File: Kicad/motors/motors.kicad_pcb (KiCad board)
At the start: 2 copper layers, 80 x 100 mm, 64 parts, among them IC101 TLV1117-50, IC201 PIC16F1778-IP, IC301 MCP2221A-ISL, K101 Battery, K201 MCU 1, K202 MCU 2, K203 ICSP, K301 FRONT, K302 MICRO USB B, K303 M20-782084x, K304 M20-782084x, K305 SERVO LEFT, K306 SERVO RIGHT, T101 DMP2305U, T102 DMP2305U

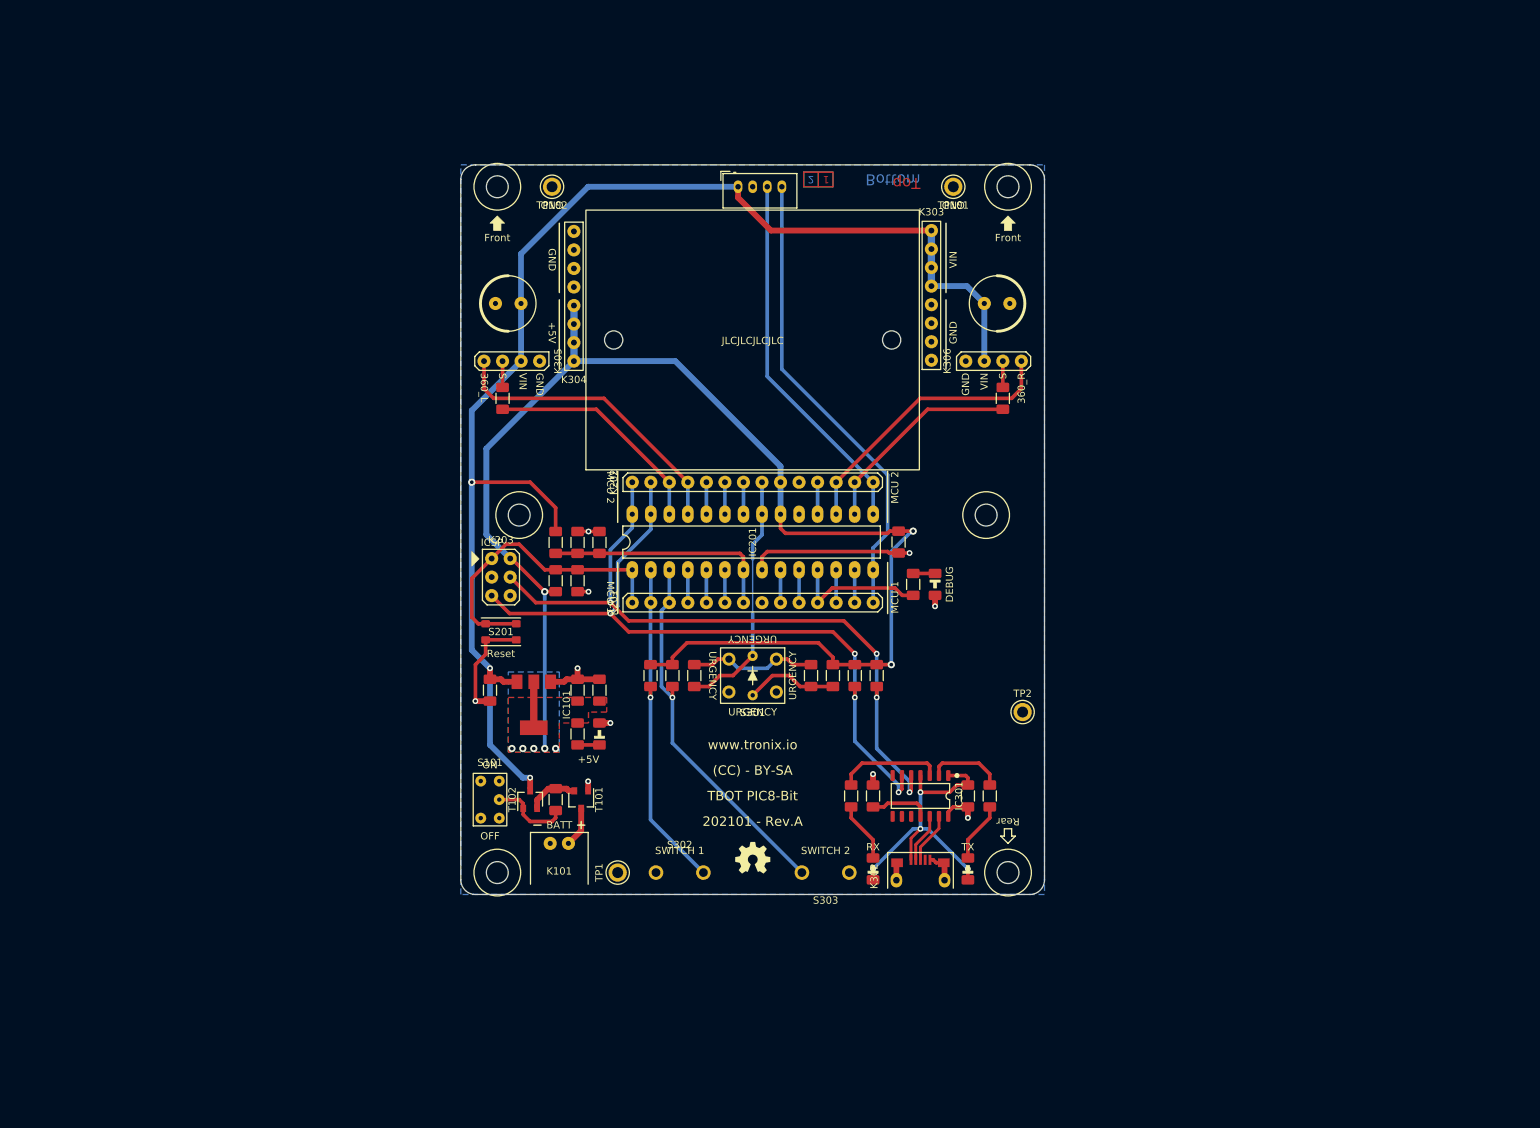
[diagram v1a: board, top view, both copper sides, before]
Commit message: Update Motors
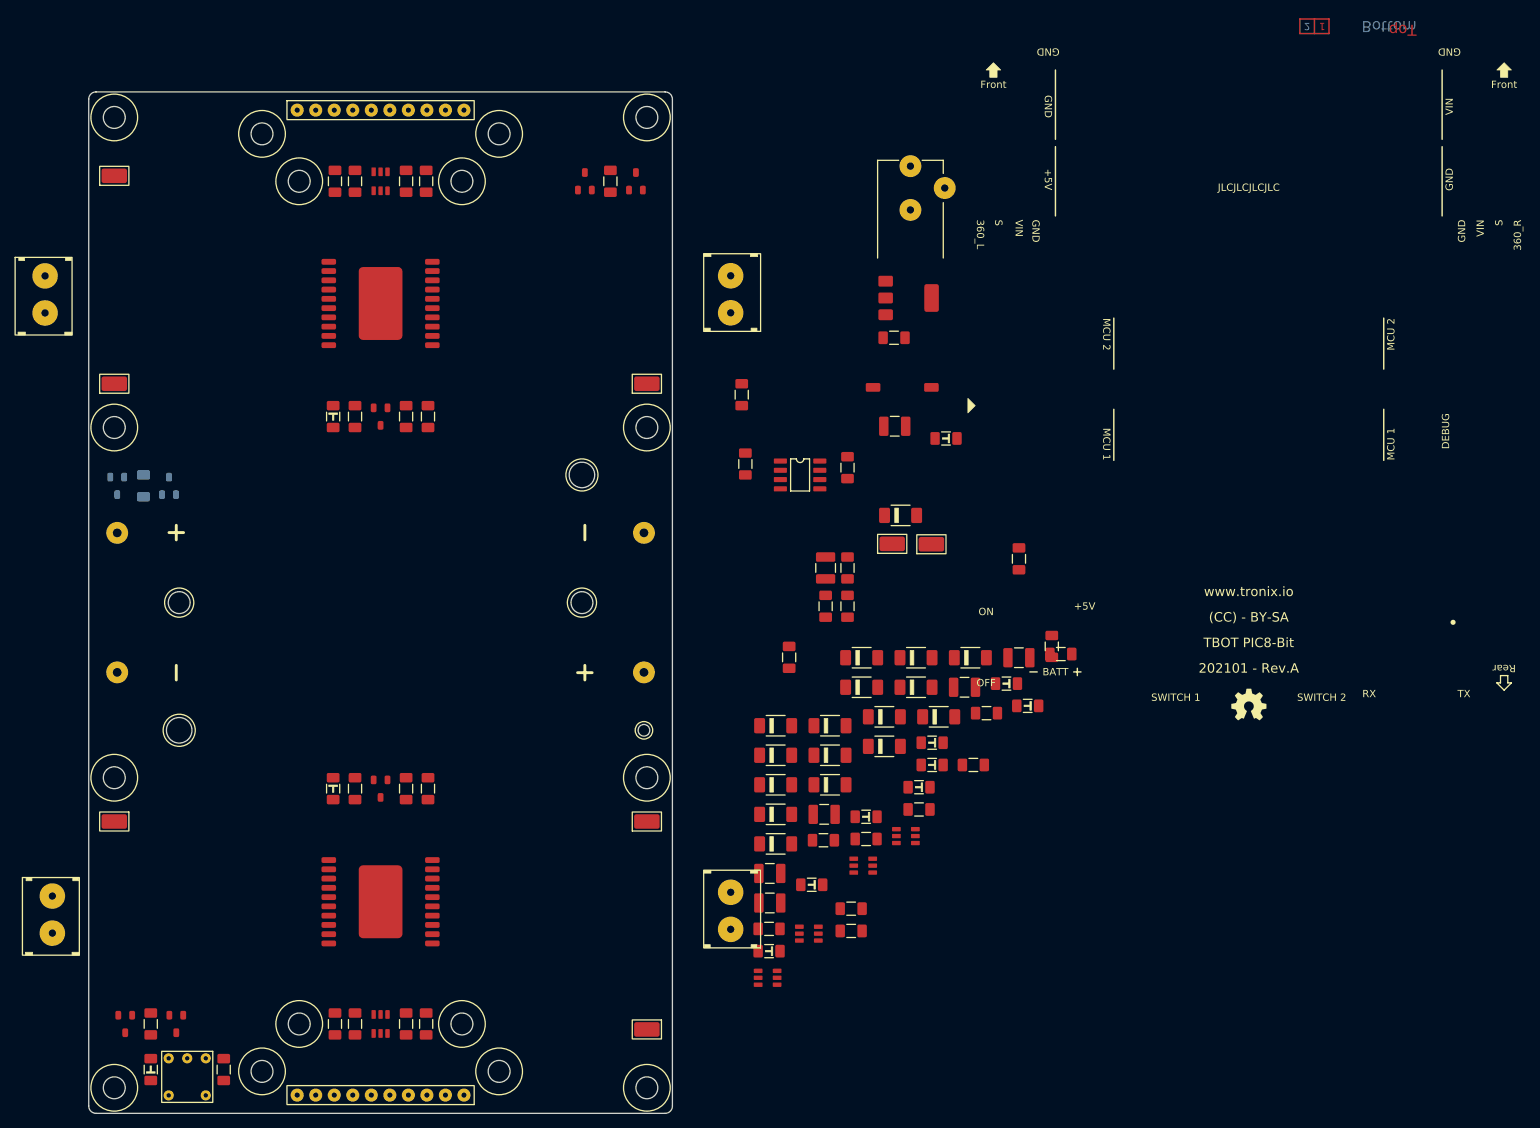
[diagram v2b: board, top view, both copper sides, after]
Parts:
- removed BB301: BREADBOARD-170, tronixALL:BREADBOARD-170
- removed C102, C104: 10µ, tronixALL:CAPACITOR_1206
- removed C103: 100n, tronixALL:CAPACITOR_1206
- removed H1, H2, H3, H4, H5, H6: MOUNTING-HOLE-MASK-3MM, tronixALL:M3-MASK
- removed IC101: TLV1117-50, tronixALL:SOT-223-3
- removed K101: Battery, tronixALL:MOLEX-5268-02
- removed K303, K304: M20-782084x, tronixALL:M20-782084x
- removed K305: SERVO LEFT, tronixALL:M20-999044x
- removed K306: SERVO RIGHT, tronixALL:M20-999044x
- removed LED302: UTX, tronixALL:LED_1206
- removed LED305: DEBUG, tronixALL:LED_1206
- removed R310, R311: 10K, tronixALL:RESISTOR_1206
- removed R314: 5K6, tronixALL:RESISTOR_1206
- removed S101: ON/OFF, tronixALL:E-SWITCH-200USPXT1A1M2RE
- removed S201: Reset, tronixALL:ALPS-SKRPAC
- removed S301: URGENCY, tronixALL:E-SWITCH-TL1240XQ1JXXX
- removed S302: SWITCH 1, tronixALL:CK-PTS635S-THT
- removed S303: SWITCH 2, tronixALL:CK-PTS635S-THT
- removed T101, T102: DMP2305U, tronixALL:SOT-23-3
- removed TP1, TP2: GND, tronixALL:KEYSTONE-5006
- added BT100: 2x18650, tronixio:KEYSTONE-1049, F.Cu at (89.0, 110.0)
- added C100: 100n, tronixio:CAPACITOR-1206, F.Cu at (153.5, 151.9)
- added C205: 100n, tronixio:CAPACITOR-1206, F.Cu at (172.1, 125.2)
- added C206: 100n, tronixio:CAPACITOR-1206, F.Cu at (155.6, 142.4)
- added C209: 100n, tronixio:CAPACITOR-1206, F.Cu at (170.2, 132.2)
- added C210: 100n, tronixio:CAPACITOR-1206, F.Cu at (142.2, 154.7)
- added C211: 1µ, tronixio:CAPACITOR-1206, F.Cu at (85.5, 84.5)
- added C212: 1µ, tronixio:CAPACITOR-1206, F.Cu at (92.5, 84.5)
- added C305: 1µ, tronixio:CAPACITOR-1206, F.Cu at (85.5, 135.5)
- added C306: 1µ, tronixio:CAPACITOR-1206, F.Cu at (92.5, 135.5)
- added D100: PMEG3030, tronixio:SOD-128, F.Cu at (160.3, 98.0)
- added D201: PMEG3030, tronixio:SOD-128, F.Cu at (143.2, 143.1)
- added D202: PMEG3030, tronixio:SOD-128, F.Cu at (154.9, 117.5)
- added D203: PMEG3030, tronixio:SOD-128, F.Cu at (162.4, 117.5)
- added D204: PMEG3030, tronixio:SOD-128, F.Cu at (169.8, 117.5)
- added D205: PMEG3030, tronixio:SOD-128, F.Cu at (143.2, 135.0)
- added D206: PMEG3030, tronixio:SOD-128, F.Cu at (158.1, 129.7)
- added D207: PMEG3030, tronixio:SOD-128, F.Cu at (165.5, 125.7)
- added D208: PMEG3030, tronixio:SOD-128, F.Cu at (143.2, 126.9)
- added D209: PMEG3030, tronixio:SOD-128, F.Cu at (150.6, 130.9)
- added D210: PMEG3030, tronixio:SOD-128, F.Cu at (158.1, 125.7)
- added D211: PMEG3030, tronixio:SOD-128, F.Cu at (154.9, 121.6)
- added D212: PMEG3030, tronixio:SOD-128, F.Cu at (150.6, 135.0)
- added D213: PMEG3030, tronixio:SOD-128, F.Cu at (150.6, 126.9)
- added D214: PMEG3030, tronixio:SOD-128, F.Cu at (143.2, 139.0)
- added D215: PMEG3030, tronixio:SOD-128, F.Cu at (143.2, 130.9)
- added D216: PMEG3030, tronixio:SOD-128, F.Cu at (162.4, 121.6)
- added H101: MOUNTING-HOLE-MASK-3MM, tronixio:M3-MASK, F.Cu at (52.5, 176.5)
- added H102: MOUNTING-HOLE-MASK-3MM, tronixio:M3-MASK, F.Cu at (72.8, 174.2)
- added H103: MOUNTING-HOLE-MASK-3MM, tronixio:M3-MASK, F.Cu at (77.8, 167.8)
- added H104: MOUNTING-HOLE-MASK-3MM, tronixio:M3-MASK, F.Cu at (100.2, 167.8)
- added H105: MOUNTING-HOLE-MASK-3MM, tronixio:M3-MASK, F.Cu at (105.2, 174.2)
- added H106: MOUNTING-HOLE-MASK-3MM, tronixio:M3-MASK, F.Cu at (125.5, 176.5)
- added H107: MOUNTING-HOLE-MASK-3MM, tronixio:M3-MASK, F.Cu at (125.5, 134.0)
- added H108: MOUNTING-HOLE-MASK-3MM, tronixio:M3-MASK, F.Cu at (125.5, 86.0)
- added H109: MOUNTING-HOLE-MASK-3MM, tronixio:M3-MASK, F.Cu at (125.5, 43.5)
- added H110: MOUNTING-HOLE-MASK-3MM, tronixio:M3-MASK, F.Cu at (105.2, 45.8)
- added H111: MOUNTING-HOLE-MASK-3MM, tronixio:M3-MASK, F.Cu at (100.2, 52.2)
- added H112: MOUNTING-HOLE-MASK-3MM, tronixio:M3-MASK, F.Cu at (77.8, 52.2)
- added H113: MOUNTING-HOLE-MASK-3MM, tronixio:M3-MASK, F.Cu at (72.8, 45.8)
- added H114: MOUNTING-HOLE-MASK-3MM, tronixio:M3-MASK, F.Cu at (52.5, 43.5)
- added H115: MOUNTING-HOLE-MASK-3MM, tronixio:M3-MASK, F.Cu at (52.5, 86.0)
- added H116: MOUNTING-HOLE-MASK-3MM, tronixio:M3-MASK, F.Cu at (52.5, 134.0)
- added IC100: BQ2057W, tronixio:SOIC-08, F.Cu at (146.5, 92.5)
- added IC202: SN74LVC1G19, tronixio:SOT-23-6, F.Cu at (142.1, 161.4)
- added IC203: SN74LVC1G19, tronixio:SOT-23-6, F.Cu at (155.2, 146.1)
- added IC204: L298P, tronixio:zzzSOPOWER-20, F.Cu at (89.0, 151.0)
- added IC205: SN74LVC1G19, tronixio:SOT-23-6, F.Cu at (147.7, 155.4)
- added IC206: SN74LVC1G19, tronixio:SOT-23-6, F.Cu at (161.0, 142.0)
- added IC207: LM3480-50, tronixio:SOT-23-3, F.Cu at (89.0, 84.5)
- added IC302: SN74LVC2G17, tronixio:SOT-23-6, F.Cu at (89.0, 167.8)
- added IC307: LM3480-33, tronixio:SOT-23-3, F.Cu at (89.0, 135.5)
- added K100: Charger, tronixio:CUI-PJ-102AH, F.Cu at (161.6, 50.2)
- added K204: MOTOR 3, tronixio:CUI-TB006-508-02BE, F.Cu at (44.0, 150.2)
- added LED100: Charging, tronixio:LED-1206, F.Cu at (166.5, 87.5)
- added LED201: Red, tronixio:LED-1206, F.Cu at (164.6, 132.2)
- added LED202: Red, tronixio:LED-1206, F.Cu at (162.8, 135.3)
- added LED203: Red, tronixio:LED-1206, F.Cu at (164.6, 129.2)
- added LED204: Red, tronixio:LED-1206, F.Cu at (177.7, 124.2)
- added LED205: Red, tronixio:LED-1206, F.Cu at (155.6, 139.3)
- added LED206: Red, tronixio:LED-1206, F.Cu at (142.2, 157.8)
- added LED207: Red, tronixio:LED-1206, F.Cu at (174.8, 121.1)
- added LED208: Red, tronixio:LED-1206, F.Cu at (148.1, 148.7)
- added LED209: +5V, tronixio:LED-1206, F.Cu at (82.5, 84.5)
- added Q100: STN790A, tronixio:SOT-223-3, F.Cu at (161.4, 68.2)
- added Q101: DMP2305U, tronixio:SOT-23-3, B.Cu at (52.9, 94.0)
- added Q102: DMP2305U, tronixio:SOT-23-3, B.Cu at (60.0, 94.0)
- added Q301: BC846B, tronixio:SOT-23-3, F.Cu at (117.0, 52.2)
- added Q302: BC846B, tronixio:SOT-23-3, F.Cu at (61.0, 167.8)
- added Q303: BC846B, tronixio:SOT-23-3, F.Cu at (124.0, 52.2)
- added Q304: BC846B, tronixio:SOT-23-3, F.Cu at (54.0, 167.8)
- added R100: 0Ω1, tronixio:RESISTOR-1210, F.Cu at (159.5, 85.8)
- added R105: 10K, tronixio:RESISTOR-1206, F.Cu at (159.4, 73.7)
- added R106: 36K, tronixio:RESISTOR-1206, F.Cu at (153.5, 155.0)
- added R107: 15K, tronixio:RESISTOR-1206, F.Cu at (67.5, 174.0)
- added R202: 10K, tronixio:RESISTOR-1206, F.Cu at (149.7, 142.6)
- added R203: 10K, tronixio:RESISTOR-1206, F.Cu at (182.2, 117.0)
- added R204: 0Ω5, tronixio:RESISTOR-1210, F.Cu at (176.5, 117.5)
- added R205: 0Ω5, tronixio:RESISTOR-1210, F.Cu at (169.0, 121.6)
- added R206: 10K, tronixio:RESISTOR-1206, F.Cu at (162.8, 138.3)
- added R207: 10K, tronixio:RESISTOR-1206, F.Cu at (138.5, 81.5)
- added R208: 10K, tronixio:RESISTOR-1210, F.Cu at (149.8, 139.0)
- added R209: 0Ω5, tronixio:RESISTOR-1210, F.Cu at (142.3, 147.1)
- added R210: 0Ω5, tronixio:RESISTOR-1210, F.Cu at (142.3, 151.2)
- added R211: 12K, tronixio:RESISTOR-1206, F.Cu at (95.5, 84.5)
- added S100: On/Off, tronixio:zzzE-SWITCH-200USPXT1A1M6RE, F.Cu at (62.5, 175.0)
- added TH100: 10K, tronixio:THERMISTOR, F.Cu at (160.5, 80.5)
- added TP100: HARWIN-S1751, tronixio:zzzHARWIN-S1751, F.Cu at (52.5, 80.0)
- added TP103: HARWIN-S1751, tronixio:zzzHARWIN-S1751, F.Cu at (52.5, 51.5)
- added TP104: HARWIN-S1751, tronixio:zzzHARWIN-S1751, F.Cu at (159.1, 101.9)
- added TP105: HARWIN-S1751, tronixio:zzzHARWIN-S1751, F.Cu at (164.5, 102.0)
- added TP201: HARWIN-S1751, tronixio:zzzHARWIN-S1751, F.Cu at (125.5, 80.0)
- added TP301: HARWIN-S1751, tronixio:zzzHARWIN-S1751, F.Cu at (125.5, 140.0)
- C101: value 100n -> 1µ; footprint tronixALL:CAPACITOR_1206 -> tronixio:CAPACITOR-1206
- C201, C202, C301: footprint tronixALL:CAPACITOR_1206 -> tronixio:CAPACITOR-1206
- C302: value 470n -> 1µ; footprint tronixALL:CAPACITOR_1206 -> tronixio:CAPACITOR-1206
- C303: value UVZ-220U-25V -> 100n; footprint tronixALL:CAPACITOR-ELECTROLYTIC-RADIAL-080-115-035 -> tronixio:CAPACITOR-1206
- C304: value UVZ-220U-25V -> 1µ; footprint tronixALL:CAPACITOR-ELECTROLYTIC-RADIAL-080-115-035 -> tronixio:CAPACITOR-1206
- IC201: value PIC16F1778-IP -> L298P; footprint tronixALL:DIP-28-W762 -> tronixio:zzzSOPOWER-20
- IC301: value MCP2221A-ISL -> SN74LVC2G17; footprint tronixALL:SOIC-SL-14 -> tronixio:SOT-23-6
- K201: value MCU 1 -> MOTOR 1; footprint tronixALL:M20-999144x -> tronixio:CUI-TB006-508-02BE
- K202: value MCU 2 -> MOTOR 2; footprint tronixALL:M20-999144x -> tronixio:CUI-TB006-508-02BE
- K203: value ICSP -> MOTOR 4; footprint tronixALL:M20-998034x -> tronixio:CUI-TB006-508-02BE
- K301: value FRONT -> Front; footprint tronixALL:JST-PH-B4B-K -> tronixio:zzHARWIN-M20-782104x
- K302: value MICRO USB B -> Rear; footprint tronixALL:FCI-USB-TYPE-B-MICRO-THT -> tronixio:zzHARWIN-M20-782104x
- LED101: footprint tronixALL:LED_1206 -> tronixio:LED-1206
- LED301: value URX -> +3V3; footprint tronixALL:LED_1206 -> tronixio:LED-1206
- R101: value 7K5 -> 0Ω1; footprint tronixALL:RESISTOR_1206 -> tronixio:RESISTOR-1210
- R102: value 100K -> 1K; footprint tronixALL:RESISTOR_1206 -> tronixio:RESISTOR-1206
- R103, R201: footprint tronixALL:RESISTOR_1206 -> tronixio:RESISTOR-1206
- R104: value 5K6 -> 1M; footprint tronixALL:RESISTOR_1206 -> tronixio:RESISTOR-1206; moved to B.Cu
- R301, R302: value 100K -> 10K; footprint tronixALL:RESISTOR_1206 -> tronixio:RESISTOR-1206
- R303: value 220R -> 10K; footprint tronixALL:RESISTOR_1206 -> tronixio:RESISTOR-1206
- R304: value 150R -> 10K; footprint tronixALL:RESISTOR_1206 -> tronixio:RESISTOR-1206
- R305, R306: value 5K6 -> 2K2; footprint tronixALL:RESISTOR_1206 -> tronixio:RESISTOR-1206
- R307: value 300R -> 33Ω; footprint tronixALL:RESISTOR_1206 -> tronixio:RESISTOR-1206
- R308: value 220R -> 33Ω; footprint tronixALL:RESISTOR_1206 -> tronixio:RESISTOR-1206
- R309: value 220R -> 6K8; footprint tronixALL:RESISTOR_1206 -> tronixio:RESISTOR-1206
- TP101, TP102: value GND -> HARWIN-S1751; footprint tronixALL:KEYSTONE-5006 -> tronixio:zzzHARWIN-S1751
- moved C304 152.3 mm to (57.5, 167.8), turned to -90 degrees
- moved TP101 144.2 mm to (52.5, 140.0)
- moved C301 119.0 mm to (85.5, 52.2)
- moved TP102 116.2 mm to (125.5, 168.5)
- moved IC301 112.1 mm to (89.0, 52.2), turned to 90 degrees
- moved R305 104.0 mm to (92.5, 52.2)
- moved R301 100.5 mm to (82.8, 52.2), turned to -90 degrees
- moved C303 99.7 mm to (92.5, 167.8), turned to 90 degrees
- moved R309 95.2 mm to (95.5, 135.5), turned to -90 degrees
- moved R306 92.4 mm to (85.5, 167.8), turned to 90 degrees
- moved K201 92.1 mm to (43.0, 65.2), turned to -90 degrees
- moved K302 90.5 mm to (77.6, 177.5)
- moved R303 87.7 mm to (95.2, 52.2), turned to -90 degrees
- moved R304 80.9 mm to (82.8, 167.8), turned to 90 degrees
- moved LED101 76.8 mm to (57.5, 174.0)
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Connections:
- C101 pad 1: RA5/BATTERY_SENSE -> VBAT
- C202 pad 1: ~{MCLR} -> VIN
- C301 pad 1: VUSB -> +3V3
- C302 pad 1: Net-(C302-Pad1) -> +3V3
- C303 pad 1: VIN -> +3V3
- C304 pad 1: VIN -> +3V3
- IC201 pad 1: ~{MCLR} -> GND
- IC201 pad 10: RA6 -> GND
- IC201 pad 11: RC0/LED -> GND
- IC201 pad 12: RC1 -> +5V
- IC201 pad 13: RC2/ENABLE -> Net-(IC203-Pad6)
- IC201 pad 14: RC3/TRIGGER -> /Driver/STOP
- IC201 pad 15: RC4/ECHO -> Net-(IC203-Pad4)
- IC201 pad 16: RC5/SERVO_R -> Net-(D203-Pad2)
- IC201 pad 17: RC6/360_R -> Net-(D204-Pad2)
- IC201 pad 18: RC7 -> (no net)
- IC201 pad 19: GND -> /Driver/M2_SENSE
- IC201 pad 2: RA0/SWITCH_1 -> /Driver/M1_SENSE
- IC201 pad 20: +5V -> GND
- IC201 pad 21: RB0/URGENCY -> (no net)
- IC201 pad 3: RA1/SWITCH_2 -> (no net)
- IC201 pad 4: RA2 -> Net-(D201-Pad2)
- IC201 pad 5: RA3 -> Net-(D202-Pad2)
- IC201 pad 6: RA4 -> VIN
- IC201 pad 7: RA5/BATTERY_SENSE -> Net-(IC202-Pad6)
- IC201 pad 8: GND -> /Driver/STOP
- IC201 pad 9: RA7 -> Net-(IC202-Pad4)
- IC301 pad 1: VUSB -> Net-(IC301-Pad1)
- IC301 pad 2: Net-(IC301-Pad2) -> GND
- IC301 pad 4: VUSB -> ENCODER_M2
- IC301 pad 5: RB7/PGD/UTX -> (no net)
- IC301 pad 6: RB6/PGC/URX -> +3V3
- K201 pad 1: ~{MCLR} -> Net-(D201-Pad2)
- K201 pad 2: RA0/SWITCH_1 -> Net-(D202-Pad2)
- K202 pad 1: RB7/PGD/UTX -> Net-(D203-Pad2)
- K202 pad 2: RB6/PGC/URX -> Net-(D204-Pad2)
- K203 pad 1: ~{MCLR} -> Net-(D209-Pad2)
- K203 pad 2: +5V -> Net-(D210-Pad2)
- K301 pad 2: GND -> /Driver/M2_SENSE
- K301 pad 3: RC4/ECHO -> /Driver/M2_SPEED
- K301 pad 4: RC3/TRIGGER -> ENCODER_M12
- K302 pad 1: VUSB -> VIN
- K302 pad 2: Net-(IC301-Pad12) -> /Driver/M3_SENSE
- K302 pad 3: Net-(IC301-Pad13) -> /Driver/M3_SPEED
- K302 pad 4: (no net) -> ENCODER_M34
- K302 pad 5: GND -> ENCODER_M3
- K302 pad 6: GND -> ENCODER_M4
- LED301 pad 1: Net-(LED301-Pad1) -> GND
- LED301 pad 2: VUSB -> Net-(LED301-Pad2)
- R101 pad 1: RA5/BATTERY_SENSE -> VCC
- R101 pad 2: VIN -> Net-(IC100-Pad1)
- R103 pad 1: GND -> VCC
- R103 pad 2: RA5/BATTERY_SENSE -> Net-(IC100-Pad4)
- R104 pad 1: Net-(LED101-Pad2) -> Net-(R104-Pad1)
- R104 pad 2: +5V -> Net-(Q101-Pad2)
- R201 pad 1: ~{MCLR} -> +3V3
- R201 pad 2: +5V -> /Driver/BRAKE
- R301 pad 1: RB7/PGD/UTX -> +3V3
- R301 pad 2: +5V -> Net-(IC301-Pad1)
- R302 pad 1: RB6/PGC/URX -> +3V3
- R302 pad 2: +5V -> Net-(IC302-Pad1)
- R303 pad 1: Net-(R303-Pad1) -> +3V3
- R303 pad 2: +5V -> Net-(IC301-Pad3)
- R304 pad 1: Net-(R304-Pad1) -> +3V3
- R304 pad 2: Net-(R303-Pad1) -> Net-(IC302-Pad3)
- R305 pad 1: Net-(IC301-Pad3) -> ENCODER_M12
- R305 pad 2: Net-(LED301-Pad1) -> Net-(Q301-Pad1)
- R306 pad 1: Net-(IC301-Pad2) -> ENCODER_M34
- R307 pad 1: Net-(R304-Pad1) -> Net-(Q301-Pad2)
- R307 pad 2: RB0/URGENCY -> GND
- R308 pad 1: RB5/SERVO_L -> Net-(Q302-Pad2)
- R308 pad 2: Net-(K305-Pad3) -> GND
- R309 pad 1: RC5/SERVO_R -> +3V3
- R309 pad 2: Net-(K306-Pad3) -> Net-(LED301-Pad2)
- TP101 pad 1: GND -> VIN
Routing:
- net +5V: track 194.5 -> 0.00 mm, vias 8 -> 0
- net VIN: track 188.5 -> 0.00 mm, vias 3 -> 0
- net RB6/PGC/URX: track 98.8 -> 0.00 mm, vias 4 -> 0
- net RB7/PGD/UTX: track 97.1 -> 0.00 mm, vias 4 -> 0
- net GND: track 67.8 -> 0.00 mm, vias 10 -> 0
- net RC3/TRIGGER: track 63.8 -> 0.00 mm
- net RA1/SWITCH_2: track 51.4 -> 0.00 mm, vias 1 -> 0
- net RC4/ECHO: track 50.9 -> 0.00 mm
- net RA0/SWITCH_1: track 46.5 -> 0.00 mm, vias 1 -> 0
- net VUSB: track 43.4 -> 0.00 mm, vias 4 -> 0
- net ~{MCLR}: track 41.7 -> 0.00 mm
- net RB4/360_L: track 41.4 -> 0.00 mm
- net RC6/360_R: track 38.9 -> 0.00 mm
- net RB0/URGENCY: track 34.1 -> 0.00 mm
- net RA5/BATTERY_SENSE: track 32.2 -> 0.00 mm
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- removed copper zone on B.Cu, net +5V
- removed copper zone on F.Cu, net +5V
- removed copper zone on B.Cu, net GND
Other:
- board size 80 x 100 mm -> 80 x 140 mm
- board text removed: "URGENCY"

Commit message: Update Motor
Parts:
- removed Q101, Q102: DMP2305U, tronixio:SOT-23-3
- removed TP104, TP105: HARWIN-S1751, tronixio:zzzHARWIN-S1751
- added C203: UVZ-470U-35V, tronixio:zzzCAPACITOR-ELECTROLYTIC-RADIAL-100-160-050, F.Cu at (65.0, 72.5)
- added C204: UVZ-470U-35V, tronixio:zzzCAPACITOR-ELECTROLYTIC-RADIAL-100-160-050, F.Cu at (113.0, 72.5)
- added C207: UVZ-470U-35V, tronixio:zzzCAPACITOR-ELECTROLYTIC-RADIAL-100-160-050, F.Cu at (65.0, 127.5)
- added C208: UVZ-470U-35V, tronixio:zzzCAPACITOR-ELECTROLYTIC-RADIAL-100-160-050, F.Cu at (113.0, 127.5)
- added H117: MOUNTING-HOLE-MASK-3MM, tronixio:M3.5, F.Cu at (75.0, 127.0)
- added H118: MOUNTING-HOLE-MASK-3MM, tronixio:M3.5, F.Cu at (103.0, 127.0)
- added H119: MOUNTING-HOLE-MASK-3MM, tronixio:M3.5, F.Cu at (103.0, 73.0)
- added H120: MOUNTING-HOLE-MASK-3MM, tronixio:M3.5, F.Cu at (75.0, 73.0)
- added IC303: OPB610, tronixio:zzzOPB-610, B.Cu at (67.5, 42.2)
- added IC304: OPB610, tronixio:zzzOPB-610, B.Cu at (110.5, 157.8)
- added IC305: OPB610, tronixio:zzzOPB-610, B.Cu at (110.5, 42.2)
- added IC306: OPB610, tronixio:zzzOPB-610, B.Cu at (67.5, 157.8)
- added T101: DMP2305U, tronixio:SOT-23-3, B.Cu at (52.9, 84.0)
- added T102: DMP2305U, tronixio:SOT-23-3, B.Cu at (60.0, 84.0)
- C100, C101, C302, C304, D100, IC100, LED100, Q100, R100, R101, R102, R103, R105, R106, R202, R203, R206, R207, TH100: moved to B.Cu
- K100: footprint tronixio:CUI-PJ-102AH -> tronixio:zzzCUI-PJ-002AH-SMT-TR; moved to B.Cu
- R208: footprint tronixio:RESISTOR-1210 -> tronixio:RESISTOR-1206
- moved G*** 142.8 mm to (66.0, 109.0)
- moved G*** 137.8 mm to (89.0, 110.5)
- moved LED201 137.2 mm to (54.0, 51.0)
- moved LED202 129.3 mm to (54.0, 65.5), turned to 180 degrees
- moved LED207 124.1 mm to (54.0, 149.5)
- moved R202 122.9 mm to (54.0, 65.5), turned to 180 degrees
- moved D201 120.2 mm to (62.5, 54.0), turned to -90 degrees
- moved R204 119.5 mm to (75.0, 54.6), turned to 180 degrees
- moved IC202 117.9 mm to (75.0, 64.5)
- moved R308 116.2 mm to (57.5, 157.8), turned to -90 degrees
- moved C209 115.0 mm to (75.0, 67.8), turned to 180 degrees
- moved D206 113.1 mm to (67.5, 62.0), turned to -90 degrees
- moved D205 108.8 mm to (62.5, 62.0), turned to -90 degrees
- moved R207 108.5 mm to (54.0, 149.5), turned to 0 degrees
- moved D202 108.1 mm to (67.5, 54.0), turned to -90 degrees
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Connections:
- net Net-(D203-Pad2) renamed /Driver/M2+
- net Net-(D204-Pad2) renamed /Driver/M2-
- net Net-(D211-Pad2) renamed /Driver/M3+
- net Net-(D212-Pad2) renamed /Driver/M3-
- D201 pad 2: Net-(D201-Pad2) -> /Driver/M1+
- D202 pad 2: Net-(D202-Pad2) -> /Driver/M1-
- D205 pad 1: Net-(D201-Pad2) -> /Driver/M1+
- D206 pad 1: Net-(D202-Pad2) -> /Driver/M1-
- D209 pad 2: Net-(D209-Pad2) -> /Driver/M4+
- D210 pad 2: Net-(D210-Pad2) -> /Driver/M4-
- D213 pad 1: Net-(D209-Pad2) -> /Driver/M4+
- D214 pad 1: Net-(D210-Pad2) -> /Driver/M4-
- IC201 pad 18: (no net) -> unconnected-(IC201-Pad18)
- IC201 pad 21: (no net) -> GND
- IC201 pad 3: (no net) -> unconnected-(IC201-Pad3)
- IC201 pad 4: Net-(D201-Pad2) -> /Driver/M1+
- IC201 pad 5: Net-(D202-Pad2) -> /Driver/M1-
- IC204 pad 18: (no net) -> unconnected-(IC204-Pad18)
- IC204 pad 21: (no net) -> GND
- IC204 pad 3: (no net) -> unconnected-(IC204-Pad3)
- IC204 pad 4: Net-(D209-Pad2) -> /Driver/M4+
- IC204 pad 5: Net-(D210-Pad2) -> /Driver/M4-
- IC301 pad 5: (no net) -> +3V3
- IC301 pad 6: +3V3 -> ENCODER_M1
- IC302 pad 5: (no net) -> +3V3
- IC302 pad 6: +3V3 -> ENCODER_M4
- K201 pad 1: Net-(D201-Pad2) -> /Driver/M1-
- K201 pad 2: Net-(D202-Pad2) -> /Driver/M1+
- K203 pad 1: Net-(D209-Pad2) -> /Driver/M4-
- K203 pad 2: Net-(D210-Pad2) -> /Driver/M4+
- LED201 pad 1: Net-(D202-Pad2) -> /Driver/M1-
- LED202 pad 2: Net-(D202-Pad2) -> /Driver/M1-
- LED205 pad 1: Net-(D210-Pad2) -> /Driver/M4-
- LED206 pad 2: Net-(D210-Pad2) -> /Driver/M4-
- R202 pad 2: Net-(D201-Pad2) -> /Driver/M1+
- R206 pad 2: Net-(D209-Pad2) -> /Driver/M4+
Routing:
- net VIN: track 0.00 -> 392.3 mm, vias 0 -> 19
- net /Driver/BRAKE: track 0.00 -> 211.8 mm, vias 0 -> 10
- net +3V3: track 0.00 -> 209.6 mm, vias 0 -> 7
- net +5V: track 0.00 -> 195.0 mm, vias 0 -> 9
- net GND: track 0.00 -> 187.3 mm, vias 0 -> 58
- net /Driver/STOP: track 0.00 -> 181.8 mm, vias 0 -> 8
- net Net-(R104-Pad1): track 0.00 -> 94.5 mm, vias 0 -> 2
- net VBAT: track 0.00 -> 77.6 mm, vias 0 -> 29
- net Net-(IC304-Pad2): track 0.00 -> 47.3 mm
- net Net-(IC303-Pad2): track 0.00 -> 47.3 mm
- net VCC: track 0.00 -> 42.1 mm, vias 0 -> 3
- net Net-(Q302-Pad1): track 0.00 -> 37.9 mm
- net Net-(Q301-Pad1): track 0.00 -> 37.6 mm
- net Net-(IC100-Pad4): track 0.00 -> 35.5 mm, vias 0 -> 3
- net /Driver/M4_SPEED: track 0.00 -> 35.5 mm, vias 0 -> 1
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- added copper zone on B.Cu, net /Driver/M1+
- added copper zone on F.Cu, net /Driver/M1+
- added copper zone on B.Cu, net /Driver/M1-
- added copper zone on F.Cu, net /Driver/M1-
- added copper zone on B.Cu, net /Driver/M2+
- added copper zone on F.Cu, net /Driver/M2+
- added copper zone on B.Cu, net /Driver/M2-
- added copper zone on F.Cu, net /Driver/M2-
- added copper zone on B.Cu, net /Driver/M3+
- added copper zone on F.Cu, net /Driver/M3+
- added copper zone on B.Cu, net /Driver/M3-
- added copper zone on F.Cu, net /Driver/M3-
- added copper zone on B.Cu, net /Driver/M4+
- added copper zone on F.Cu, net /Driver/M4+
- added copper zone on B.Cu, net /Driver/M4-
- added copper zone on F.Cu, net /Driver/M4-
- added copper zone on B.Cu, net GND
- added copper zone on F.Cu, net GND
- added copper zone on B.Cu, net VBAT
- added copper zone on F.Cu, net VBAT
- added copper zone on B.Cu, net VIN
- added copper zone on F.Cu, net VIN
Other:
- board text added: "+3V3"
- board text added: "202201 - Rev.A"
- board text added: "9V - 1A"
- board text added: "BRAKE"
- board text added: "Charge"
- board text added: "EM1"
- board text added: "EM12"
- board text added: "EM2"
- board text added: "EM3"
- board text added: "EM34"
- board text added: "EM4"
- board text added: "M1"
- board text added: "M1SN"
- board text added: "M1SPD"
- board text added: "M2"
- board text added: "M2SN"
- board text added: "M2SPD"
- board text added: "M3"
- board text added: "M3SN"
- board text added: "M3SPD"
- board text added: "M4"
- board text added: "M4SN"
- board text added: "M4SPD"
- board text added: "MOTOR 1"
- board text added: "MOTOR 2"
- board text added: "MOTOR 3"
- board text added: "MOTOR 4"
- board text added: "STOP"
- board text added: "TCAR Motor Board - L298P"
- board text added: "TCAR Motor Board L298P - Rev.A - (01/2022) - Scale 100%"
- board text added: "VBAT"
- board text removed: "202101 - Rev.A"
- board text removed: "360_L"
- board text removed: "360_R"
- board text removed: "BATT"
- board text removed: "DEBUG"
- board text removed: "MCU 1"
- board text removed: "MCU 2"
- board text removed: "RX"
- board text removed: "S"
- board text removed: "SWITCH 1"
- board text removed: "SWITCH 2"
- board text removed: "TBOT PIC8-Bit"
- board text removed: "TX"

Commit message: Update
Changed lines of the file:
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@@
       (net 3 "VBAT") (pinfunction "C") (pintype "passive"))
     (pad "2" smd roundrect locked (at 3.15 0 90) (size 2 3.8) (layers "B.Cu" "B.Paste" "B.Mask") (roundrect_rratio 0.15)
-      (net 3 "VBAT") (pinfunction "C") (pintype "passive"))
+      (net 3 "VBAT") (pinfunction "C") (pintype "passive") (zone_connect 2))
     (pad "3" smd roundrect locked (at -3.15 -2.3 90) (size 2 1.5) (layers "B.Cu" "B.Paste" "B.Mask") (roundrect_rratio 0.15)
       (net 18 "Net-(IC100-Pad1)") (pinfunction "E") (pintype "passive"))
@@
     (effects (font (size 1.3 1.3) (thickness 0.15)) (justify mirror))
   )
-  (gr_text "JLCJLCJLCJLC" (at 89 47) (layer "B.SilkS")
-    (effects (font (size 1 1) (thickness 0.15)) (justify mirror))
-  )
-  (gr_text "M1" (at 74.75 76.5) (layer "B.SilkS")
+  (gr_text "M1" (at 75 69.5) (layer "B.SilkS")
     (effects (font (size 1.3 1.3) (thickness 0.15)) (justify mirror))
   )
@@
     (effects (font (size 1.3 1.3) (thickness 0.15)) (justify mirror))
   )
-  (gr_text "M2" (at 103 76.5) (layer "B.SilkS")
+  (gr_text "M2" (at 103 69.5) (layer "B.SilkS")
     (effects (font (size 1.3 1.3) (thickness 0.15)) (justify mirror))
   )
-  (gr_text "www.tronix.io" (at 89 115) (layer "B.SilkS")
+  (gr_text "www.tronix.io" (at 89 115.5) (layer "B.SilkS")
     (effects (font (size 1.3 1.3) (thickness 0.15)) (justify mirror))
   )
@@
     (effects (font (size 1 1) (thickness 0.15)) (justify left))
   )
+  (gr_text "JLCJLCJLCJLC" (at 89 101.5) (layer "F.SilkS")
+    (effects (font (size 1 1) (thickness 0.15)))
+  )
   (gr_text "GND" (at 77.6 34 270) (layer "F.SilkS")
     (effects (font (size 1 1) (thickness 0.15)) (justify left))
@@
     (effects (font (size 1.3 1.3) (thickness 0.15)))
   )
-  (gr_text "M4" (at 103 130.5) (layer "F.SilkS")
+  (gr_text "M4" (at 103 123.5) (layer "F.SilkS")
     (effects (font (size 1.3 1.3) (thickness 0.15)))
   )
@@
     (effects (font (size 1 1) (thickness 0.15)) (justify right))
   )
-  (gr_text "M3" (at 75 130.5) (layer "F.SilkS")
+  (gr_text "M3" (at 75 123.5) (layer "F.SilkS")
     (effects (font (size 1.3 1.3) (thickness 0.15)))
   )
@@
     (pts (xy 129 170) (xy 129 30))
     (height 3)
-    (gr_text "140.00 mm" (at 130.85 100 90) (layer "Dwgs.User")
+    (gr_text "140.00 mm" (at 133.5 100 90) (layer "Dwgs.User")
       (effects (font (size 1 1) (thickness 0.15)))
     )
     (format (units 2) (units_format 1) (precision 2))
-    (style (thickness 0.15) (arrow_length 1) (text_position_mode 0) (extension_height 0.58642) (extension_offset 0.5) keep_text_aligned)
+    (style (thickness 0.15) (arrow_length 1) (text_position_mode 2) (extension_height 0.58642) (extension_offset 0.5) keep_text_aligned)
   )
   (segment (start 73.5 132.5) (end 73.5 134.5) (width 0.8) (layer "F.Cu") (net 1))
